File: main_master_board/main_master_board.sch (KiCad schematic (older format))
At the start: 10 parts, among them J1 RJ45, P5 Mounting Holes, P6 Mounting Holes, P7 Mounting Holes, P8 Mounting Holes, U1 NRF24L01+

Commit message: Moved library files to dedicated folder. Added support for Edison and Open-Q 410 boards.
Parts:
- removed D2, D3: D_Schottky, TO-220-3:D-Pack-3, symbol D_Schottky
- removed F1: 3413.0328.22, dp_devices:dp_devices-C1206, symbol Polyfuse
- removed J1: RJ45, RJ45-SMD:TE-338088-outline, symbol RJ45
- removed U1: NRF24L01+, pinhead:pinhead-2X04%2f90, symbol NRF24L01+
- added F1: 3413.0328.22, dp_devices:dp_devices-C1206, symbol Fuse
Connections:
- net labels removed: V12_cur, V12_volt, V_hebi1, V_hebi2
- wire segments 42 -> 40
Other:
- note removed: "Bettery Reverse\nCurrent Protection"
- note removed: "Dummy place holders"
- note removed: "Probably should change \nto a replaceable fuse\n154005DRT?"
- moved on the sheet: P5, P7
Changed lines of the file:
@@
 LIBS:USB_CONSOL-SchDoc-cache
 LIBS:VBAT_PROTECTION_REGS-SchDoc-cache
-LIBS:LMR16020
-LIBS:TPS832130SIL
 LIBS:TPS754
-LIBS:TPS61089
 LIBS:FDS4935A
 LIBS:Si1900DL
@@
 LIBS:xal6030-182mec
 LIBS:decaWave
+LIBS:conn_2x50
+LIBS:conn_open_q_x2
+LIBS:LMR16020
+LIBS:TPS61089
 LIBS:TPS61232DRC
+LIBS:TPS832130SIL
+LIBS:SS4-50-3.00-X-D
 LIBS:main_master_board-cache
 EELAYER 25 0
@@
 $Descr A4 11693 8268
 encoding utf-8
-Sheet 1 5
+Sheet 1 6
 Title ""
 Date ""
@@
 F6 "Vbackup" I L 1470 4280 60
 F7 "GND24" I L 1470 5480 60
-F8 "V12_cur" O R 2580 4690 60
-F9 "V12_volt" O R 2580 4820 60
-F10 "V5_cur" O R 2580 4960 60
-F11 "V5_volt" O R 2580 5080 60
-F12 "3V3_cur" O R 2580 5210 60
-F13 "3V3_volt" O R 2580 5360 60
-F14 "GND" O R 2580 5500 60
+F8 "V5_cur" O R 2580 4960 60
+F9 "V5_volt" O R 2580 5080 60
+F10 "3V3_cur" O R 2580 5210 60
+F11 "3V3_volt" O R 2580 5360 60
+F12 "GND" O R 2580 5500 60
 $EndSheet
 Text Label 940  4280 0    60   ~ 0
@@
 Vmain
 $Comp
-L Polyfuse F1
-U 1 1 587008FC
-P 3100 970
-F 0 "F1" V 3000 970 50  0000 C CNN
-F 1 "3413.0328.22" V 3200 970 50  0000 C CNN
-F 2 "dp_devices:dp_devices-C1206" H 3150 770 50  0001 L CNN
-F 3 "http://datasheet.octopart.com/3413.0328.22-Schurter-datasheet-8645987.pdf" H 3100 970 50  0001 C CNN
-	1    3100 970
-	0    1    1    0
-$EndComp
-$Comp
 L ZENERsmall D1
 U 1 1 58700903
@@
 	1    0    0    -1
 $EndComp
-Text Notes 3030 830  0    60   ~ 0
-Probably should change \nto a replaceable fuse\n154005DRT?
 Text Notes 2730 1590 0    60   ~ 0
 Transient Voltage Suppessor
@@
 Text Notes 3560 1470 0    60   ~ 0
 Circuits can take 48V, \nexcept TSV diode
-$Comp
-L D_Schottky D3
-U 1 1 58700918
-P 10100 3470
-F 0 "D3" H 10100 3570 50  0000 C CNN
-F 1 "D_Schottky" H 10100 3370 50  0000 C CNN
-F 2 "TO-220-3:D-Pack-3" H 10100 3470 50  0001 C CNN
-F 3 "http://datasheet.octopart.com/STPS5H100B-TR-STMicroelectronics-datasheet-5318140.pdf" H 10100 3470 50  0001 C CNN
-	1    10100 3470
-	-1   0    0    1
-$EndComp
 Text Label 2670 970  0    60   ~ 0
 V24_in
-Text Label 10290 3470 0    60   ~ 0
-V_hebi1
-$Comp
-L D_Schottky D2
-U 1 1 58700925
-P 10090 3760
-F 0 "D2" H 10090 3860 50  0000 C CNN
-F 1 "D_Schottky" H 10090 3660 50  0000 C CNN
-F 2 "TO-220-3:D-Pack-3" H 10090 3760 50  0001 C CNN
-F 3 "http://datasheet.octopart.com/STPS5H100B-TR-STMicroelectronics-datasheet-5318140.pdf" H 10090 3760 50  0001 C CNN
-	1    10090 3760
-	-1   0    0    1
-$EndComp
-Text Label 10280 3760 0    60   ~ 0
-V_hebi2
-Text Notes 9660 3300 0    60   ~ 0
-Bettery Reverse\nCurrent Protection
 Text Label 7360 3190 0    60   ~ 0
 Vmain
@@
 Text Notes 530  1580 0    60   ~ 0
 Two Grounds to separate \nmotor ground and electronics ground
-Text Label 9670 3470 0    60   ~ 0
-Vmotors
-Text Label 9660 3760 0    60   ~ 0
-Vmotors
 Text Label 2620 4030 0    60   ~ 0
 V12
@@
 	1    0    0    -1
 $EndComp
-Text Label 2610 4690 0    60   ~ 0
-V12_cur
-Text Label 2610 4820 0    60   ~ 0
-V12_volt
 Text Label 2610 4960 0    60   ~ 0
 V5_cur
@@
 L CONN_01X01 P7
 U 1 1 58767C4C
-P 10920 670
-F 0 "P7" H 10920 770 50  0000 C CNN
-F 1 "Mounting Holes" V 11020 790 50  0000 C CNN
-F 2 "Mounting_Holes:MountingHole_3.2mm_M3_Pad" H 10920 670 50  0001 C CNN
-F 3 "" H 10920 670 50  0000 C CNN
-	1    10920 670
+P 10920 610
+F 0 "P7" H 10920 710 50  0000 C CNN
+F 1 "Mounting Holes" V 11020 710 50  0000 C CNN
+F 2 "Mounting_Holes:MountingHole_3.2mm_M3_Pad" H 10920 610 50  0001 C CNN
+F 3 "" H 10920 610 50  0000 C CNN
+	1    10920 610
 	0    -1   -1   0
 $EndComp
@@
 L CONN_01X01 P5
 U 1 1 58767F4D
-P 10700 670
-F 0 "P5" H 10700 770 50  0000 C CNN
-F 1 "Mounting Holes" V 10800 670 50  0001 C CNN
-F 2 "Mounting_Holes:MountingHole_3.2mm_M3_Pad" H 10700 670 50  0001 C CNN
-F 3 "" H 10700 670 50  0000 C CNN
-	1    10700 670
+P 10700 610
+F 0 "P5" H 10700 710 50  0000 C CNN
+F 1 "Mounting Holes" V 10800 610 50  0001 C CNN
+F 2 "Mounting_Holes:MountingHole_3.2mm_M3_Pad" H 10700 610 50  0001 C CNN
+F 3 "" H 10700 610 50  0000 C CNN
+	1    10700 610
 	0    -1   -1   0
 $EndComp
@@
 	0    1    1    0
 $EndComp
-Wire Wire Line
-	1120 690  1120 790
-Wire Wire Line
-	1470 4280 920  4280
-Wire Wire Line
-	1470 4030 1160 4030
-Wire Wire Line
-	3250 970  3890 970
-Wire Wire Line
-	3370 970  3370 1010
-Connection ~ 3370 970
-Wire Wire Line
-	3370 1210 3370 1270
-Wire Wire Line
-	2950 970  2660 970
-Wire Wire Line
-	9950 3470 9630 3470
-Wire Wire Line
-	10250 3470 10600 3470
-Wire Wire Line
-	9940 3760 9620 3760
-Wire Wire Line
-	10240 3760 10590 3760
-Wire Wire Line
-	7340 3190 7630 3190
-Wire Wire Line
-	620  700  620  750
-Wire Wire Line
-	620  750  1570 750
-Connection ~ 1120 750
-Wire Wire Line
-	1570 750  1570 690
-Wire Wire Line
-	1360 690  1360 750
-Connection ~ 1360 750
-Wire Wire Line
-	890  700  890  750
-Connection ~ 890  750
-Wire Wire Line
-	960  1200 960  1140
-Wire Wire Line
-	960  1140 1250 1140
-Wire Wire Line
-	1250 1140 1250 1200
-Connection ~ 1120 1140
-Wire Wire Line
-	2580 4030 2810 4030
-Wire Wire Line
-	2580 4280 2810 4280
-Wire Wire Line
-	2570 4530 2810 4530
-Wire Wire Line
-	7630 3330 7340 3330
-Wire Wire Line
-	2580 5500 2800 5500
-Wire Wire Line
-	2800 5500 2800 5610
-Wire Wire Line
-	2580 5360 3080 5360
-Wire Wire Line
-	2580 5210 3080 5210
-Wire Wire Line
-	2580 5080 3080 5080
-Wire Wire Line
-	2580 4960 3080 4960
-Wire Wire Line
-	2580 4820 3080 4820
-Wire Wire Line
-	2580 4690 3080 4690
-Wire Wire Line
-	8950 3240 9330 3240
-Wire Wire Line
-	7630 4020 7520 4020
-Wire Wire Line
-	7520 4020 7520 4080
-Wire Wire Line
-	7270 4100 7270 3900
-Wire Wire Line
-	7270 3900 7630 3900
-Wire Wire Line
-	7630 3740 7210 3740
-Wire Wire Line
-	7630 3610 7210 3610
-Wire Wire Line
-	7630 3480 7210 3480
-Wire Notes Line
-	10500 480  10500 1160
-Wire Notes Line
-	10500 1160 11210 1160
-Wire Wire Line
-	1230 5620 1230 5480
-Wire Wire Line
-	1230 5480 1470 5480
-$Comp
-L NRF24L01+ U1
-U 1 1 58784E3D
-P 8820 6320
-F 0 "U1" H 8870 6270 60  0000 C CNN
-F 1 "NRF24L01+" H 9070 6770 60  0000 C CNN
-F 2 "pinhead:pinhead-2X04%2f90" H 8820 6320 60  0001 C CNN
-F 3 "" H 8820 6320 60  0000 C CNN
-	1    8820 6320
-	1    0    0    -1
-$EndComp
-Text Notes 9060 5060 0    60   ~ 0
-Dummy place holders
-Wire Notes Line
-	11210 4920 8330 4920
-Wire Notes Line
-	8330 4920 8330 6520
 $Sheet
-S 4360 3080 1740 1620
+S 4900 1960 1740 1620
 U 5878C64D
 F0 "uC_and_Sensors" 60
@@
 F0 "main_connectors" 60
 F1 "../connectors.sch" 60
+F2 "V24_in" O R 4030 2380 60
+F3 "Vbackup_in" O R 4030 2570 60
+F4 "Vmotors" I L 2730 2390 60
 $EndSheet
-$Comp
-L RJ45 J1
-U 1 1 5876EB4E
-P 10400 5770
-F 0 "J1" H 10600 6270 50  0000 C CNN
-F 1 "RJ45" H 10250 6270 50  0000 C CNN
-F 2 "RJ45-SMD:TE-338088-outline" H 10400 5770 50  0001 C CNN
-F 3 "" H 10400 5770 50  0000 C CNN
-	1    10400 5770
-	1    0    0    -1
-$EndComp
+$Sheet
+S 4590 4800 1950 1590
+U 587AA41C
+F0 "snapdragon_edison" 60
+F1 "snapdragon_edison.sch" 60
+$EndSheet
+$Comp
+L Fuse F1
+U 1 1 587AE04C
+P 3100 970
+F 0 "F1" V 3180 970 50  0000 C CNN
+F 1 "3413.0328.22" V 3025 970 50  0000 C CNN
+F 2 "dp_devices:dp_devices-C1206" V 3030 970 50  0001 C CNN
+F 3 "http://datasheet.octopart.com/3413.0328.22-Schurter-datasheet-8645987.pdf" H 3100 970 50  0001 C CNN
+	1    3100 970
+	0    -1   -1   0
+$EndComp
+Wire Wire Line
+	1120 690  1120 790
+Wire Wire Line
+	1470 4280 920  4280
+Wire Wire Line
+	1470 4030 1160 4030
+Wire Wire Line
+	3250 970  3890 970
+Wire Wire Line
+	3370 970  3370 1010
+Connection ~ 3370 970
+Wire Wire Line
+	3370 1210 3370 1270
+Wire Wire Line
+	2950 970  2660 970
+Wire Wire Line
+	7340 3190 7630 3190
+Wire Wire Line
+	620  700  620  750
+Wire Wire Line
+	620  750  1570 750
+Connection ~ 1120 750
+Wire Wire Line
+	1570 750  1570 690
+Wire Wire Line
+	1360 690  1360 750
+Connection ~ 1360 750
+Wire Wire Line
+	890  700  890  750
+Connection ~ 890  750
+Wire Wire Line
+	960  1200 960  1140
+Wire Wire Line
+	960  1140 1250 1140
+Wire Wire Line
+	1250 1140 1250 1200
+Connection ~ 1120 1140
+Wire Wire Line
+	2580 4030 2810 4030
+Wire Wire Line
+	2580 4280 2810 4280
+Wire Wire Line
+	2570 4530 2810 4530
+Wire Wire Line
+	7630 3330 7340 3330
+Wire Wire Line
+	2580 5500 2800 5500
+Wire Wire Line
+	2800 5500 2800 5610
+Wire Wire Line
+	2580 5360 3080 5360
+Wire Wire Line
+	2580 5210 3080 5210
+Wire Wire Line
+	2580 5080 3080 5080
+Wire Wire Line
+	2580 4960 3080 4960
+Wire Wire Line
+	8950 3240 9330 3240
+Wire Wire Line
+	7630 4020 7520 4020
+Wire Wire Line
+	7520 4020 7520 4080
+Wire Wire Line
+	7270 4100 7270 3900
+Wire Wire Line
+	7270 3900 7630 3900
+Wire Wire Line
+	7630 3740 7210 3740
+Wire Wire Line
+	7630 3610 7210 3610
+Wire Wire Line
+	7630 3480 7210 3480
+Wire Notes Line
+	10500 480  10500 1160
+Wire Notes Line
+	10500 1160 11210 1160
+Wire Wire Line
+	1230 5620 1230 5480
+Wire Wire Line
+	1230 5480 1470 5480
+Wire Wire Line
+	10700 860  11140 860
+Wire Wire Line
+	10700 810  10700 900
+Connection ~ 10700 860
+Wire Wire Line
+	10920 810  10920 900
+Connection ~ 10920 860
+$Comp
+L GND #PWR015
+U 1 1 587B1461
+P 11140 940
+F 0 "#PWR015" H 11140 690 50  0001 C CNN
+F 1 "GND" H 11140 790 50  0000 C CNN
+F 2 "" H 11140 940 50  0000 C CNN
+F 3 "" H 11140 940 50  0000 C CNN
+	1    11140 940
+	1    0    0    -1
+$EndComp
+Wire Wire Line
+	11140 860  11140 940
 $EndSCHEMATC

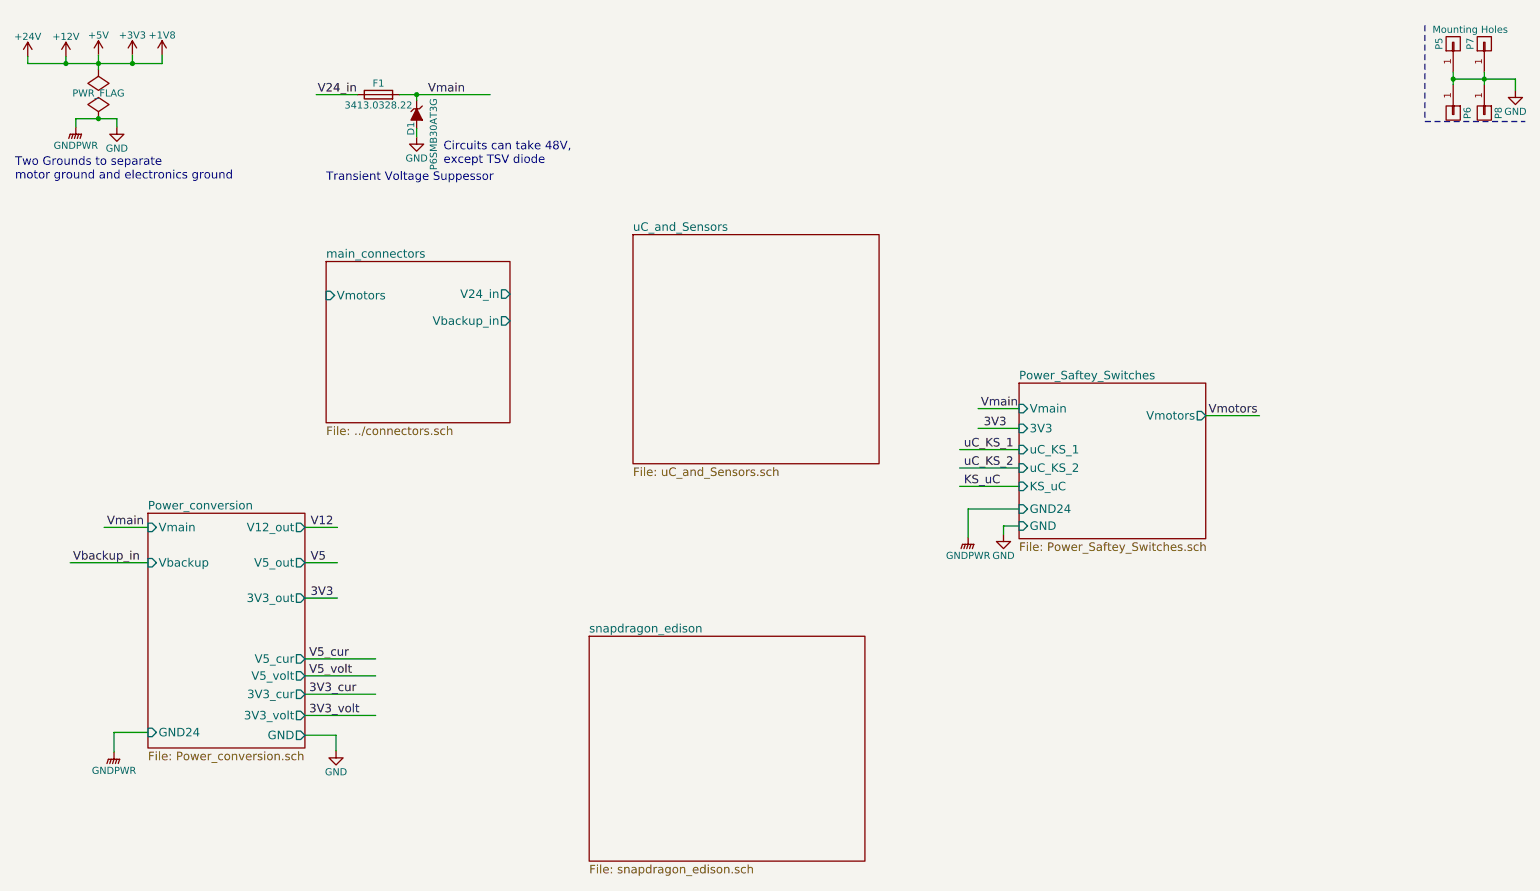
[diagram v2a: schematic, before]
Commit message: Started hooking up the dsPIC uC
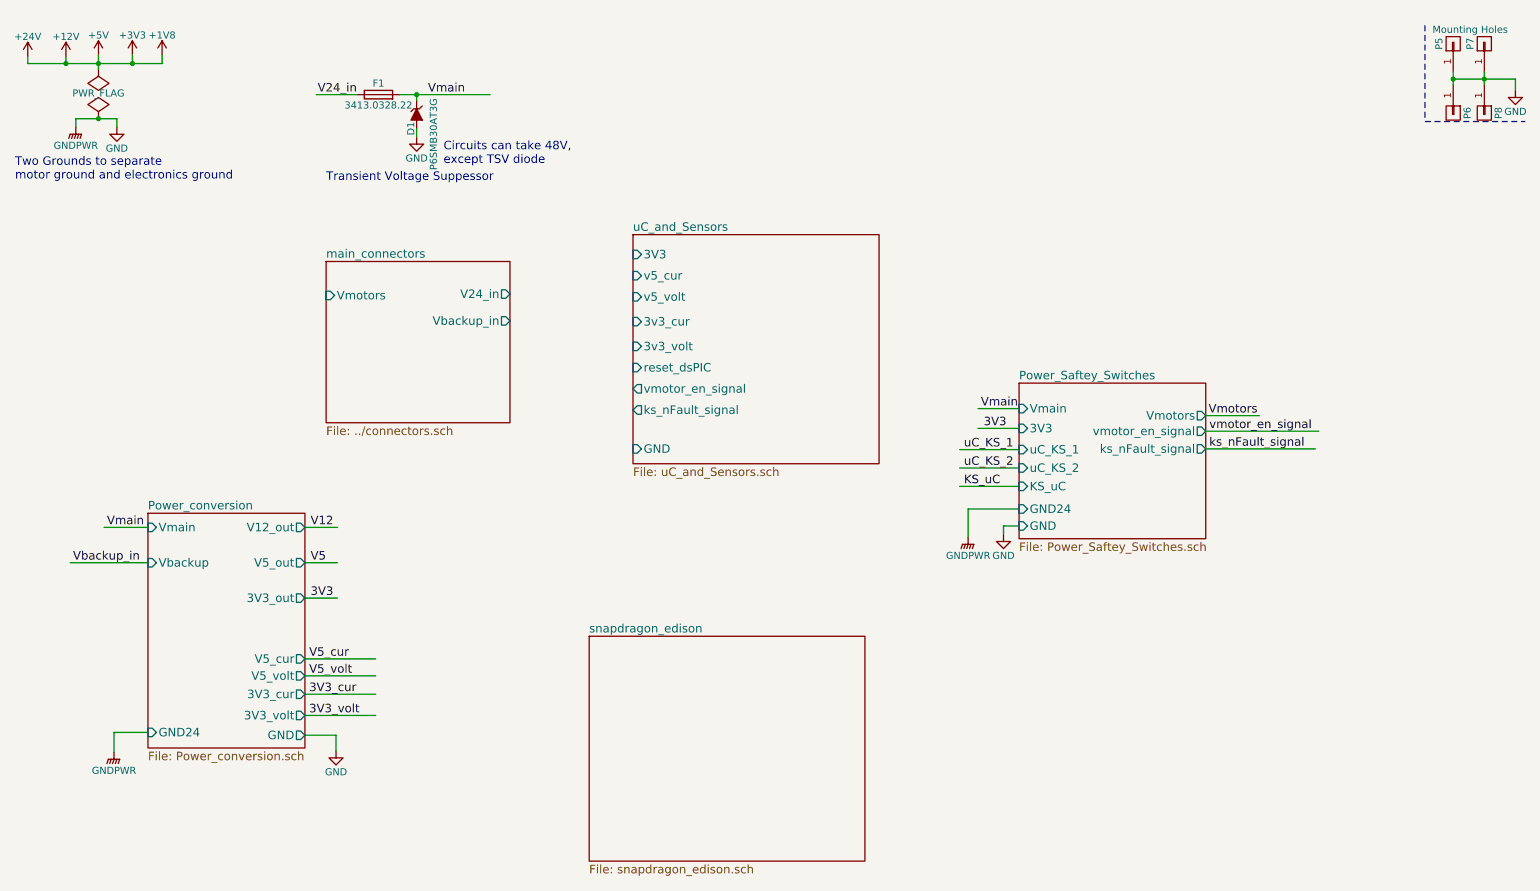
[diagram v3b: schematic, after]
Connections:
- net labels added: ks_nFault_signal, vmotor_en_signal
- wire segments 40 -> 51
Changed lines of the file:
@@
 LIBS:EDISON-SchDoc-cache
 LIBS:ETHERNET_USB_HUB-SchDoc-cache
-LIBS:PIC-SchDoc-cache
 LIBS:RF-SchDoc-cache
-LIBS:topsheet_Controller-SchDoc-cache
 LIBS:topsheet_Master-SchDoc-cache
-LIBS:topsheet_Power-SchDoc-cache
 LIBS:USB_CONSOL-SchDoc-cache
 LIBS:VBAT_PROTECTION_REGS-SchDoc-cache
+LIBS:PIC-SchDoc-cache
+LIBS:topsheet_Controller-SchDoc-cache
+LIBS:topsheet_Power-SchDoc-cache
 LIBS:TPS754
 LIBS:FDS4935A
@@
 LIBS:TPS832130SIL
 LIBS:SS4-50-3.00-X-D
+LIBS:74xgxx
+LIBS:ac-dc
+LIBS:actel
+LIBS:allegro
+LIBS:Altera
+LIBS:analog_devices
+LIBS:battery_management
+LIBS:bbd
+LIBS:brooktre
+LIBS:cmos_ieee
+LIBS:dc-dc
+LIBS:diode
+LIBS:elec-unifil
+LIBS:ESD_Protection
+LIBS:ftdi
+LIBS:gennum
+LIBS:graphic
+LIBS:hc11
+LIBS:ir
+LIBS:Lattice
+LIBS:logo
+LIBS:maxim
+LIBS:mechanical
+LIBS:microchip_dspic33dsc
+LIBS:microchip_pic10mcu
+LIBS:microchip_pic12mcu
+LIBS:microchip_pic16mcu
+LIBS:microchip_pic18mcu
+LIBS:microchip_pic32mcu
+LIBS:motor_drivers
+LIBS:motors
+LIBS:msp430
+LIBS:nordicsemi
+LIBS:nxp_armmcu
+LIBS:onsemi
+LIBS:Oscillators
+LIBS:Power_Management
+LIBS:powerint
+LIBS:pspice
+LIBS:references
+LIBS:relays
+LIBS:rfcom
+LIBS:sensors
+LIBS:silabs
+LIBS:stm8
+LIBS:stm32
+LIBS:supertex
+LIBS:switches
+LIBS:transf
+LIBS:ttl_ieee
+LIBS:video
+LIBS:wiznet
+LIBS:Worldsemi
+LIBS:Xicor
+LIBS:zetex
+LIBS:Zilog
 LIBS:main_master_board-cache
 EELAYER 25 0
@@
 F8 "KS_uC" I L 7630 3740 60
 F9 "GND24" I L 7630 3900 60
+F10 "vmotor_en_signal" O R 8950 3350 60
+F11 "ks_nFault_signal" O R 8950 3475 60
 $EndSheet
 Text Label 1180 4030 0    60   ~ 0
@@
 F0 "uC_and_Sensors" 60
 F1 "uC_and_Sensors.sch" 60
+F2 "3V3" I L 4900 2100 60
+F3 "GND" I L 4900 3475 60
+F4 "v5_cur" I L 4900 2250 60
+F5 "v5_volt" I L 4900 2400 60
+F6 "3v3_cur" I L 4900 2575 60
+F7 "3v3_volt" I L 4900 2750 60
+F8 "reset_dsPIC" I L 4900 2900 60
+F9 "vmotor_en_signal" O L 4900 3050 60
+F10 "ks_nFault_signal" O L 4900 3200 60
 $EndSheet
 $Sheet
@@
 $EndComp
 Wire Wire Line
-	1120 690  1120 790
+	1120 690  1120 750
+Wire Wire Line
+	1120 750  1120 790
 Wire Wire Line
 	1470 4280 920  4280
@@
 	1470 4030 1160 4030
 Wire Wire Line
-	3250 970  3890 970
+	3250 970  3370 970
+Wire Wire Line
+	3370 970  3890 970
 Wire Wire Line
 	3370 970  3370 1010
@@
 	620  700  620  750
 Wire Wire Line
-	620  750  1570 750
+	620  750  890  750
+Wire Wire Line
+	890  750  1120 750
+Wire Wire Line
+	1120 750  1360 750
+Wire Wire Line
+	1360 750  1570 750
 Connection ~ 1120 750
 Wire Wire Line
@@
 	960  1200 960  1140
 Wire Wire Line
-	960  1140 1250 1140
+	960  1140 1120 1140
+Wire Wire Line
+	1120 1140 1250 1140
 Wire Wire Line
 	1250 1140 1250 1200
@@
 	1230 5480 1470 5480
 Wire Wire Line
-	10700 860  11140 860
-Wire Wire Line
-	10700 810  10700 900
+	10700 860  10920 860
+Wire Wire Line
+	10920 860  11140 860
+Wire Wire Line
+	10700 810  10700 860
+Wire Wire Line
+	10700 860  10700 900
 Connection ~ 10700 860
 Wire Wire Line
-	10920 810  10920 900
+	10920 810  10920 860
+Wire Wire Line
+	10920 860  10920 900
 Connection ~ 10920 860
 $Comp
@@
 Wire Wire Line
 	11140 860  11140 940
+Wire Wire Line
+	8950 3350 9750 3350
+Text Label 8975 3350 0    60   ~ 0
+vmotor_en_signal
+Text Label 8975 3475 0    60   ~ 0
+ks_nFault_signal
+Wire Wire Line
+	8950 3475 9725 3475
 $EndSCHEMATC

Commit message: Started adding support for a new snapdragon board. Dart0410
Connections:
- wire segments 51 -> 42
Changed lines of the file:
@@
 LIBS:FDS4935A
 LIBS:Si1900DL
-LIBS:Amplifiers
-LIBS:Connectors
-LIBS:DataStorage
-LIBS:Diodes
-LIBS:Microprocessors
-LIBS:MiscellaneousDevices
-LIBS:Passives
-LIBS:PMOD
-LIBS:PowerComponents
-LIBS:RepeaterParts
-LIBS:RF_OEM_Parts
 LIBS:Sensors
-LIBS:TransistorParts
 LIBS:LP3852-3.3
 LIBS:0s102011ma1qn1
@@
 LIBS:xal5050-562meb
 LIBS:xal6030-182mec
-LIBS:decaWave
 LIBS:conn_2x50
 LIBS:conn_open_q_x2
@@
 LIBS:ac-dc
 LIBS:actel
-LIBS:allegro
 LIBS:Altera
 LIBS:analog_devices
@@
 LIBS:logo
 LIBS:maxim
-LIBS:mechanical
 LIBS:microchip_dspic33dsc
 LIBS:microchip_pic10mcu
@@
 LIBS:microchip_pic32mcu
 LIBS:motor_drivers
-LIBS:motors
 LIBS:msp430
 LIBS:nordicsemi
@@
 LIBS:ttl_ieee
 LIBS:video
-LIBS:wiznet
 LIBS:Worldsemi
 LIBS:Xicor
-LIBS:zetex
 LIBS:Zilog
 LIBS:main_master_board-cache
@@
 $EndComp
 Wire Wire Line
-	1120 690  1120 750
-Wire Wire Line
-	1120 750  1120 790
+	1120 690  1120 790
 Wire Wire Line
 	1470 4280 920  4280
@@
 	1470 4030 1160 4030
 Wire Wire Line
-	3250 970  3370 970
-Wire Wire Line
-	3370 970  3890 970
+	3250 970  3890 970
 Wire Wire Line
 	3370 970  3370 1010
@@
 	620  700  620  750
 Wire Wire Line
-	620  750  890  750
-Wire Wire Line
-	890  750  1120 750
-Wire Wire Line
-	1120 750  1360 750
-Wire Wire Line
-	1360 750  1570 750
+	620  750  1570 750
 Connection ~ 1120 750
 Wire Wire Line
@@
 	960  1200 960  1140
 Wire Wire Line
-	960  1140 1120 1140
-Wire Wire Line
-	1120 1140 1250 1140
+	960  1140 1250 1140
 Wire Wire Line
 	1250 1140 1250 1200
@@
 	1230 5480 1470 5480
 Wire Wire Line
-	10700 860  10920 860
-Wire Wire Line
-	10920 860  11140 860
-Wire Wire Line
-	10700 810  10700 860
-Wire Wire Line
-	10700 860  10700 900
+	10700 860  11140 860
+Wire Wire Line
+	10700 810  10700 900
 Connection ~ 10700 860
 Wire Wire Line
-	10920 810  10920 860
-Wire Wire Line
-	10920 860  10920 900
+	10920 810  10920 900
 Connection ~ 10920 860
 $Comp

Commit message: Lots of stuff
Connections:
- net labels added: cpu_SCL, cpu_SDA, prog_cts, prog_rts, prog_rx, prog_tx, reset_dsPIC
- wire segments 42 -> 59
